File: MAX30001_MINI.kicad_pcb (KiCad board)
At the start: 4 copper layers, 46.5 x 38.3 mm, 67 parts, among them J1 Conn_01x01, J2 Conn_01x01, J3 Conn_01x01, J4 Conn_01x12, U1 ADP151_3V3, U2 MAX30001CWV_T, U3 ADP151_1V8, U4 SIT1533AI-H4-DCC-32.768E

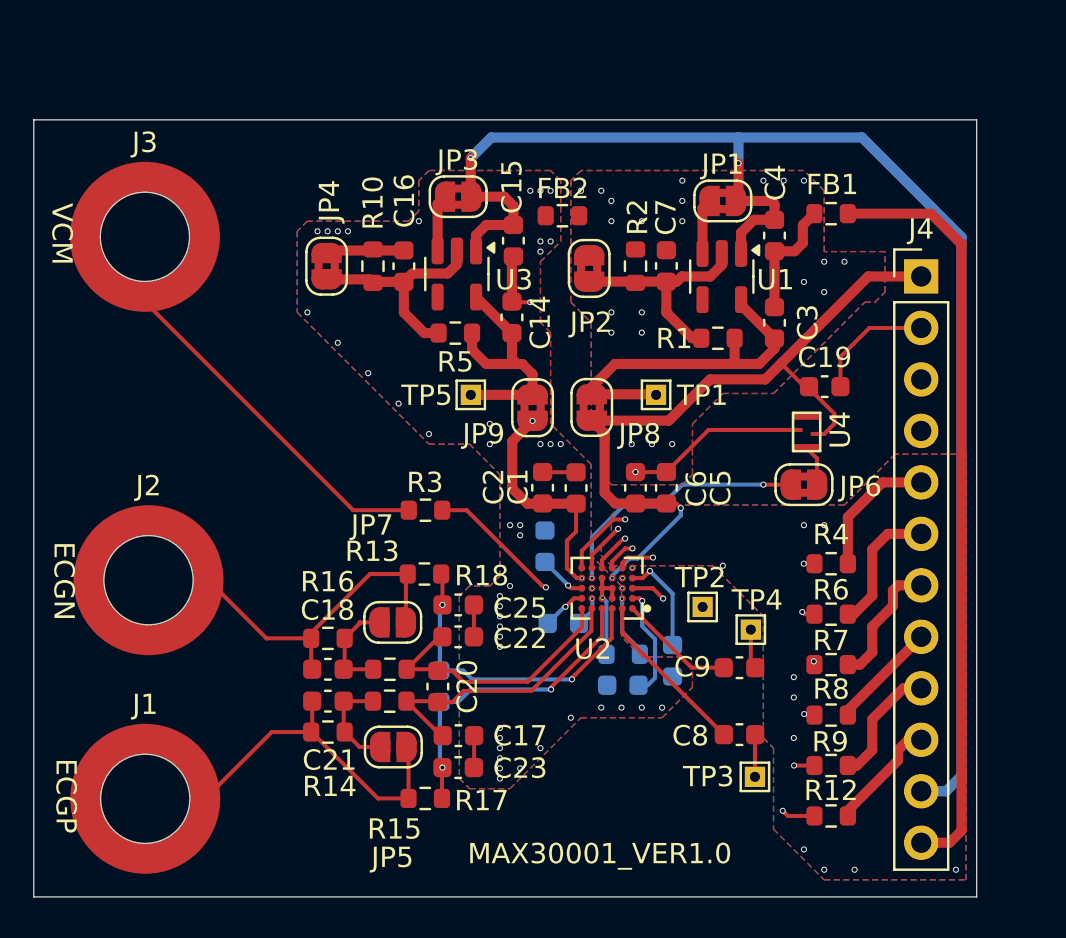
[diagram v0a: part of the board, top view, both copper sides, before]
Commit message: [fix] Fixed issue DRVP/DRVN net nodes not connected
Fixed the issue where DRVP/DRVN net nodes were not connected.
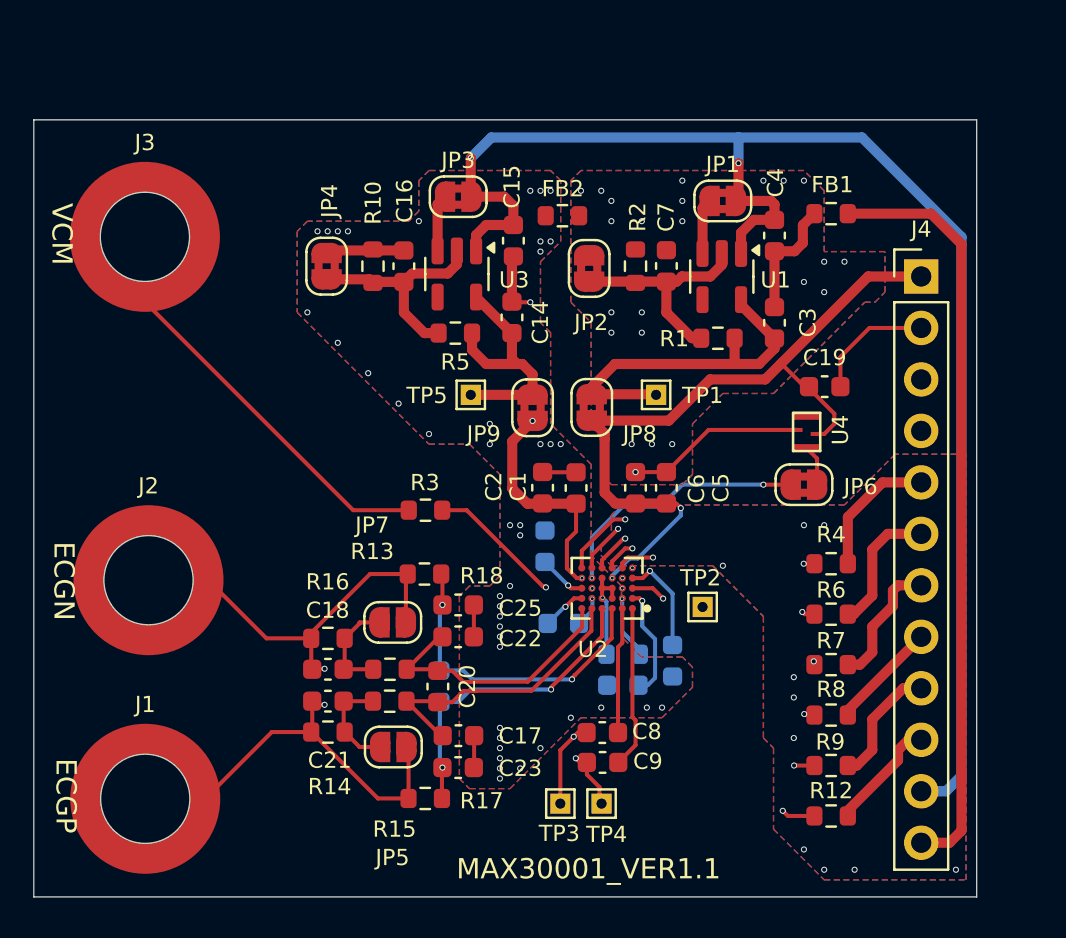
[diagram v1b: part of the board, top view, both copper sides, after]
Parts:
- moved TP4 11.3 mm to (185.0, 135.7)
- moved TP3 9.69 mm to (183.0, 135.7)
- moved C9 8.22 mm to (185.1, 133.7), turned to 180 degrees
- moved C8 6.77 mm to (185.1, 132.2), turned to 180 degrees
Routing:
- net ECGN ELECTRODE: track 18.6 -> 35.1 mm, vias 0 -> 2
- net ECGP ELECTRODE: track 18.9 -> 34.0 mm, vias 0 -> 2
- net Net-(U2-DRVP): track 5.72 -> 8.01 mm
- net Net-(U2-DRVN): track 8.30 -> 6.21 mm
- net GNDA: vias 46 -> 45
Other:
- board text added: "MAX30001_VER1.1"
- board text removed: "MAX30001_VER1.0"
